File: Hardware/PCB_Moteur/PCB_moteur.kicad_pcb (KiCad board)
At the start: 2 copper layers, 60 x 120 mm, 191 parts, among them J1 XT30PW-F, J10 Conn_01x02, J11 Conn_01x02, J12 Conn_01x02, J13 Conn_01x02, J14 Conn_01x02, J15 Conn_01x02, J16 Conn_01x06_Pin, J17 Screw_Terminal_01x04, J18 Screw_Terminal_01x04, J19 Screw_Terminal_01x04, J2 Conn_01x06_Pin, J3 Conn_01x03_Socket, J4 Conn_01x03_Socket, J5 Conn_01x03_Socket, J6 Conn_01x03_Socket, J7 Conn_01x02, J8 Conn_01x02, J9 Conn_01x02, Q1 SI5442DU-T1-GE3, Q2 SI5442DU-T1-GE3, Q3 MMBT3904, Q4 SI7617DN-T1-GE3, U1 L6981N33DR, U2 STM32F103CBT6, U3 MCP1802T-5002I/OT, U4 LSF0204PWR, U5 ISOW1044, U6 LM393, U7 INA125UA/2K5, U8 INA125UA/2K5, U9 MAX6612MXK

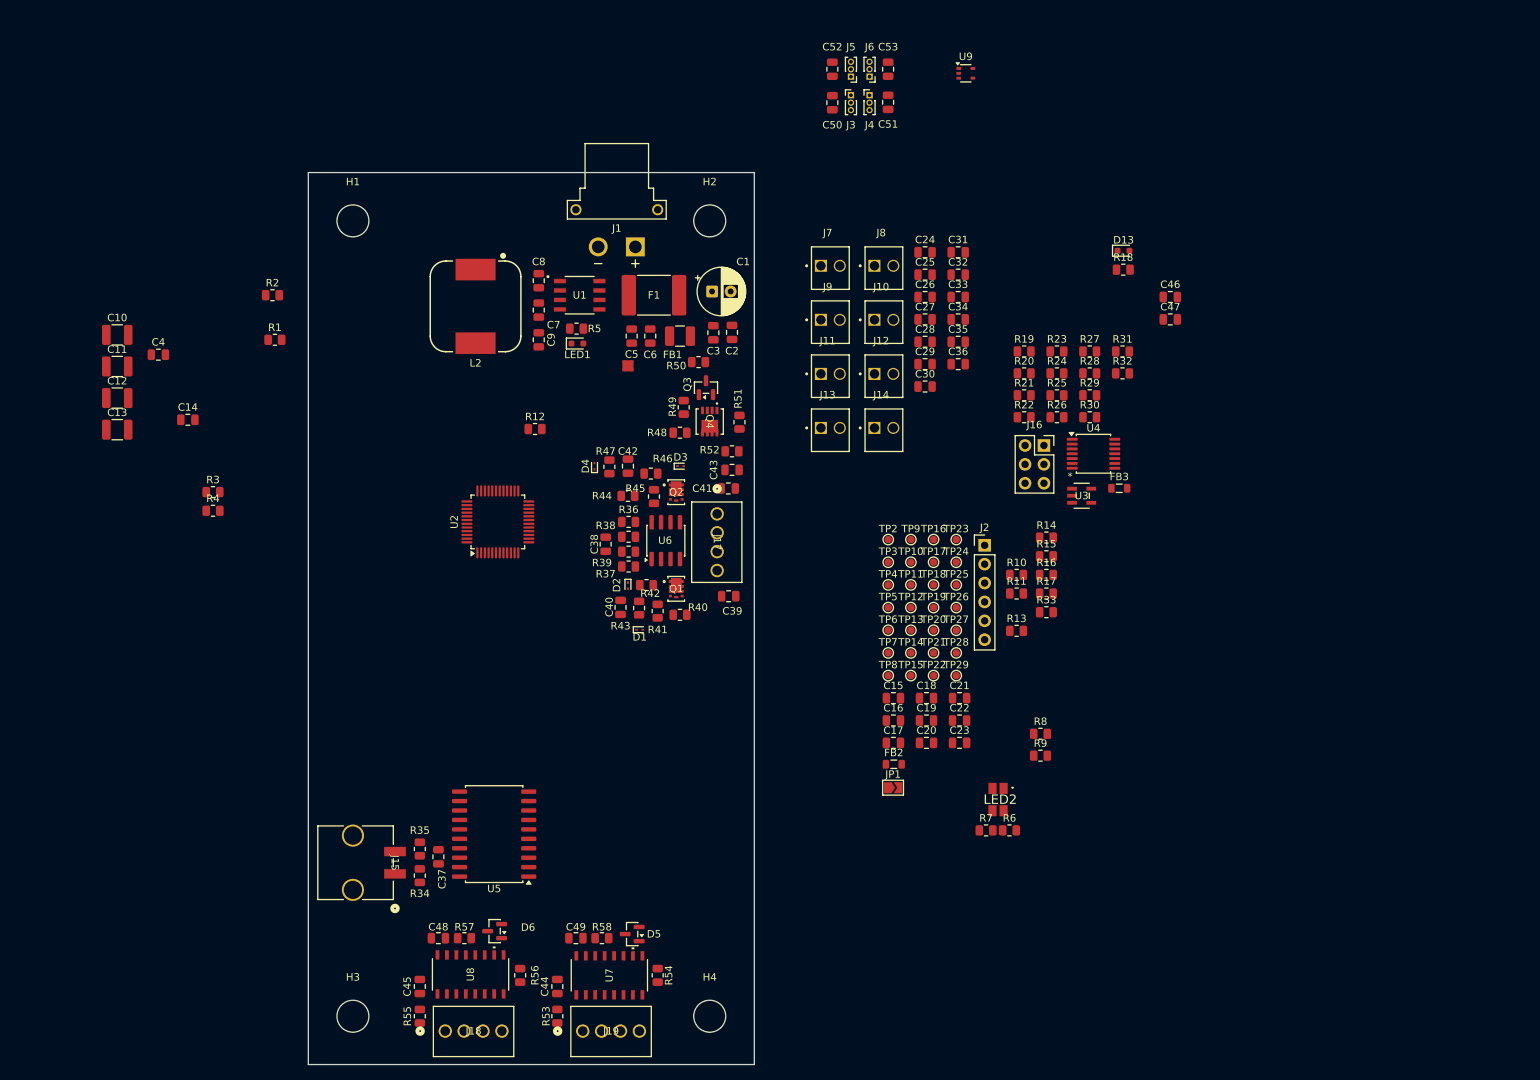
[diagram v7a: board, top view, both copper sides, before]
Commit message: wip: fin layout CAN et interface servo
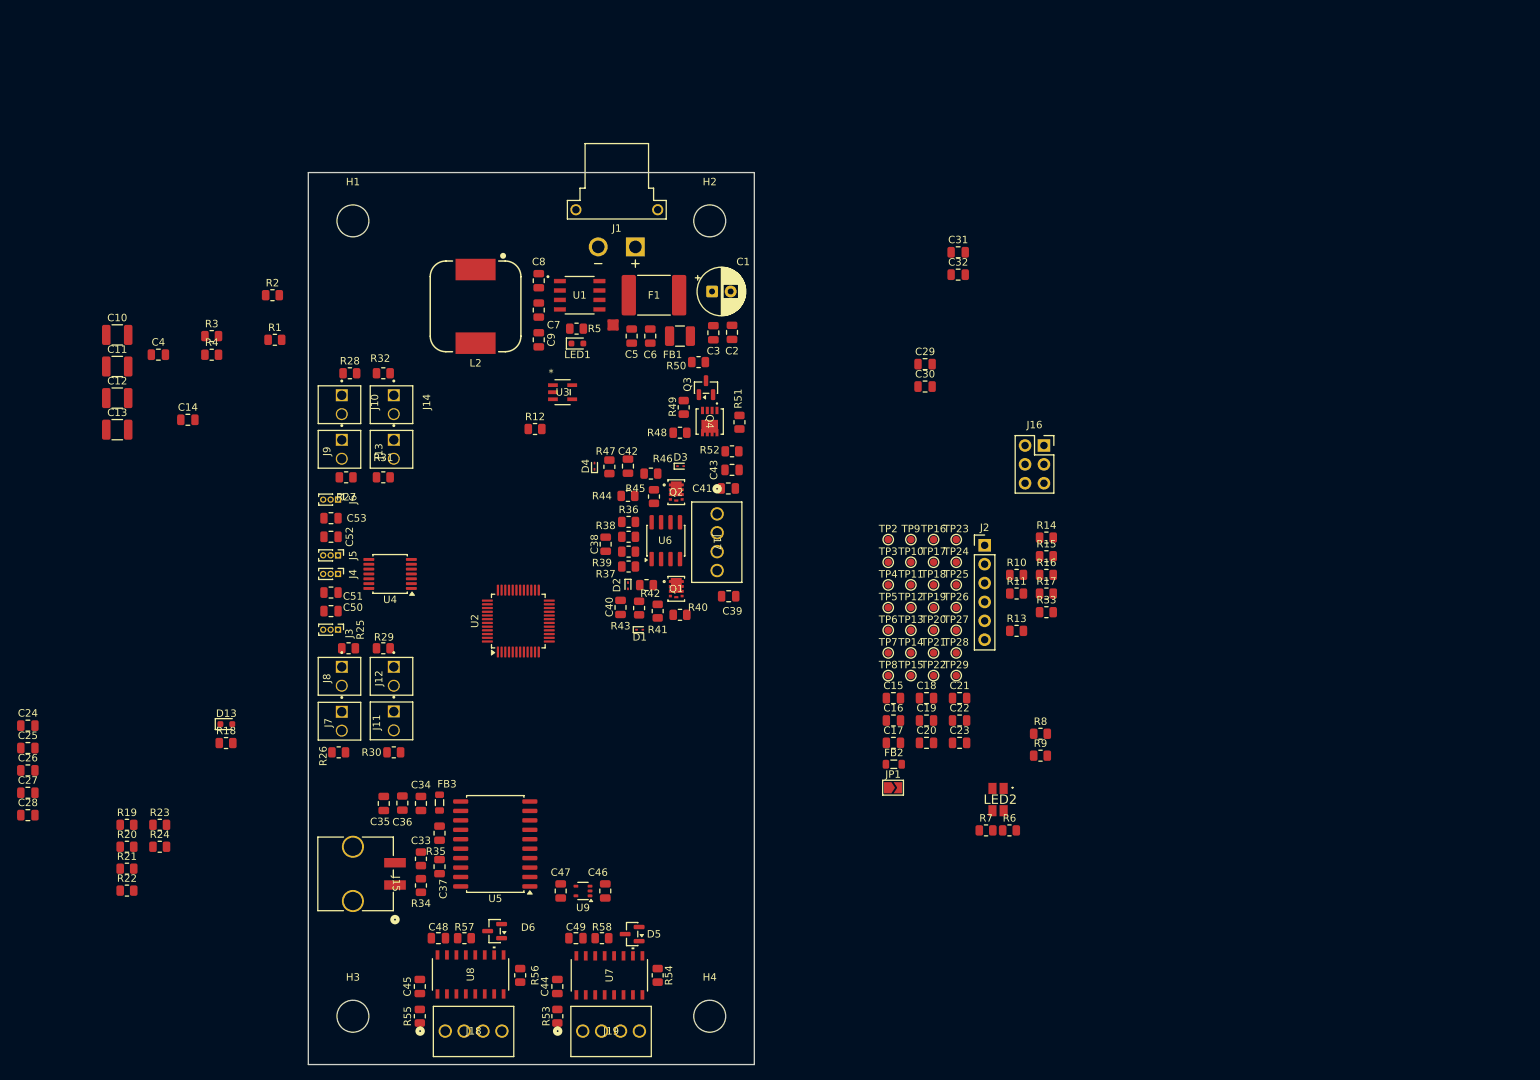
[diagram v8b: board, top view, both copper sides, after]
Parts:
- moved D13 136.5 mm to (72.0, 107.2)
- moved R19 136.5 mm to (58.6, 120.8)
- moved R20 136.5 mm to (58.6, 123.7)
- moved R21 136.5 mm to (58.6, 126.7)
- moved R23 136.5 mm to (63.0, 120.8)
- moved R24 136.5 mm to (63.0, 123.7)
- moved C24 136.5 mm to (45.3, 107.4)
- moved C25 136.5 mm to (45.3, 110.4)
- moved C26 136.5 mm to (45.3, 113.4)
- moved C27 136.5 mm to (45.3, 116.4)
- moved C28 136.5 mm to (45.3, 119.5)
- moved R18 136.5 mm to (71.9, 109.8)
- moved R22 136.5 mm to (58.6, 129.6)
- moved U9 121.5 mm to (120.0, 129.7), turned to 180 degrees
- moved C47 112.4 mm to (117.0, 129.7), turned to -90 degrees
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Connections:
- U2 pad 33: Servo1_Open -> Servo2_Open
- U2 pad 38: Servo1_Close -> Servo2_Close
- U2 pad 40: Servo2_Open -> Servo1_Open
- U2 pad 41: Servo2_Close -> Servo1_Close
